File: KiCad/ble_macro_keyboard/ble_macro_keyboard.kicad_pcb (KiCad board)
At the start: 2 copper layers, 91 x 55 mm, 38 parts, among them IC1 ADP3338AKCZ-3.3-RL, J1 Conn_01x03_Male, Q1 IRLML6402, SW1 SW_SPDT, SW10 SW_Push, SW11 SW_Push, SW12 SW_Push, SW13 SW_Push, SW14 SW_Push, SW2 SW_Push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

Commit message: [fix] Vsysラベルを3.3vへ修正
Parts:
- moved C2 55.2 mm to (235.2, -128.5)
- moved C1 54.4 mm to (196.7, -114.3)
- moved R7 39.3 mm to (199.1, -111.8), turned to 0 degrees
- moved C4 33.8 mm to (197.6, -127.0), turned to 90 degrees
- moved C6 13.7 mm to (174.8, -113.8), turned to 0 degrees
- moved D2 10.2 mm to (208.8, -122.9)
- moved R3 10.2 mm to (201.8, -122.9)
- moved R4 10.2 mm to (198.0, -122.9)
- moved R1 10.2 mm to (201.8, -127.0)
- moved R2 10.2 mm to (201.7, -125.0)
- moved C5 9.71 mm to (186.5, -113.8), turned to 0 degrees
- moved D1 9.65 mm to (208.8, -115.8)
- moved R5 9.65 mm to (208.8, -113.3)
- moved IC1 6.68 mm to (191.0, -125.0)
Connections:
- C4 pad 1: Vsys -> +3.3V
- IC1 pad 2: Vsys -> +3.3V
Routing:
- net Net-(D2-Pad3): track 0.90 -> 0.00 mm

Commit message: [update] GND以外パターン接続
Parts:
- moved R5 39.5 mm to (171.3, -126.0)
- moved D1 39.2 mm to (172.2, -130.0), turned to 180 degrees
- moved R7 28.6 mm to (171.3, -118.4)
- moved C1 26.4 mm to (171.3, -121.4), turned to 0 degrees
- moved C6 23.7 mm to (192.1, -130.0)
- moved C5 17.6 mm to (179.8, -130.0), turned to 180 degrees
- moved IC1 16.2 mm to (204.7, -116.3)
- moved C2 14.7 mm to (243.3, -116.3), turned to 90 degrees
- moved R6 13.9 mm to (185.9, -131.1)
- moved U1 13.5 mm to (185.9, -127.5)
- moved C3 11.4 mm to (185.9, -118.4), turned to 0 degrees
- moved C4 9.04 mm to (204.7, -121.4), turned to 0 degrees
- moved Q1 8.64 mm to (185.9, -114.8)
- moved J1 6.62 mm to (238.8, -116.3), turned to 90 degrees
- moved R1 4.82 mm to (203.3, -131.6)
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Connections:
- U2 pad 10: LED_R -> KeySW_read_04
- U2 pad 11: KeySW_read_12 -> KeySW_read_08
- U2 pad 12: KeySW_read_08 -> KeySW_read_12
- U2 pad 15: KeySW_read_04 -> setSW_read
- U2 pad 7: setSW_read -> LED_G
- U2 pad 8: LED_G -> LED_B
- U2 pad 9: LED_B -> LED_R
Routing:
- net KeySW_read_12: track 0.00 -> 136.6 mm
- net KeySW_read_08: track 0.00 -> 113.3 mm
- net Net-(C2-Pad1): track 0.00 -> 97.2 mm
- net KeySW_read_04: track 0.00 -> 90.5 mm
- net Net-(C3-Pad1): track 0.00 -> 79.0 mm, vias 0 -> 1
- net +5V: track 0.00 -> 70.3 mm, vias 0 -> 2
- net setSW_read: track 0.00 -> 68.7 mm
- net KeySW_read_11: track 0.00 -> 65.8 mm
- net KeySW_read_10: track 0.00 -> 58.4 mm
- net Net-(IC1-Pad3): track 0.00 -> 57.5 mm, vias 0 -> 1
- net KeySW_read_09: track 0.00 -> 53.1 mm
- net Battery_thermistor: track 0.00 -> 53.1 mm
- net KeySW_read_07: track 0.00 -> 40.3 mm
- net KeySW_read_06: track 0.00 -> 36.2 mm
- net +3.3V: track 0.00 -> 35.3 mm
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
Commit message: [add] ライブラリ及び回路図にNPTH_8mmを追加
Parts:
- added REF**: NPTH_8mm, Ble_keyboard:NPTH_8mm, F.Cu at (19.0, -32.0)
- moved REF** 233.1 mm to (40.0, 46.0)
- moved REF** 232.9 mm to (-40.0, 46.0)
- moved REF** 231.5 mm to (40.0, -41.0)
- moved REF** 231.3 mm to (-40.0, -41.0)
- moved C1 231.1 mm to (-37.4, -22.4)
- moved C2 231.1 mm to (34.5, -17.3)
- moved C3 231.1 mm to (-22.9, -19.3)
- moved C5 231.1 mm to (-29.0, -31.0)
- moved C6 231.1 mm to (-16.7, -31.0)
- moved D2 231.1 mm to (0.00, -28.4)
- moved Q1 231.1 mm to (-22.9, -15.7)
- moved R1 231.1 mm to (-5.45, -32.5)
- moved R3 231.1 mm to (-5.45, -28.4)
- moved R4 231.1 mm to (-9.26, -28.4)
- moved R6 231.1 mm to (-22.9, -32.0)
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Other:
- board size 91 x 55 mm -> 88 x 95 mm

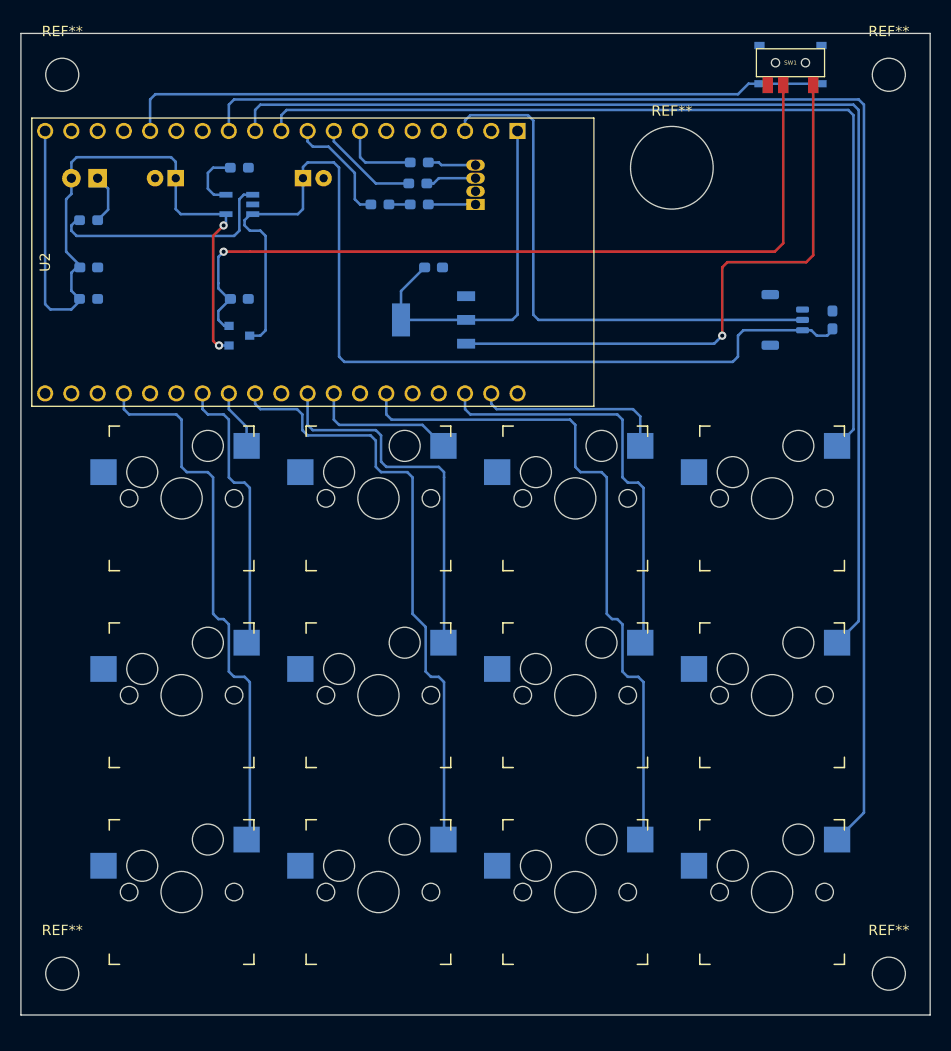
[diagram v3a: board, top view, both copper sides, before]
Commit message: [fix] Ble_keyboardフットプリントライブラリのSWがGNDに接続するように解決
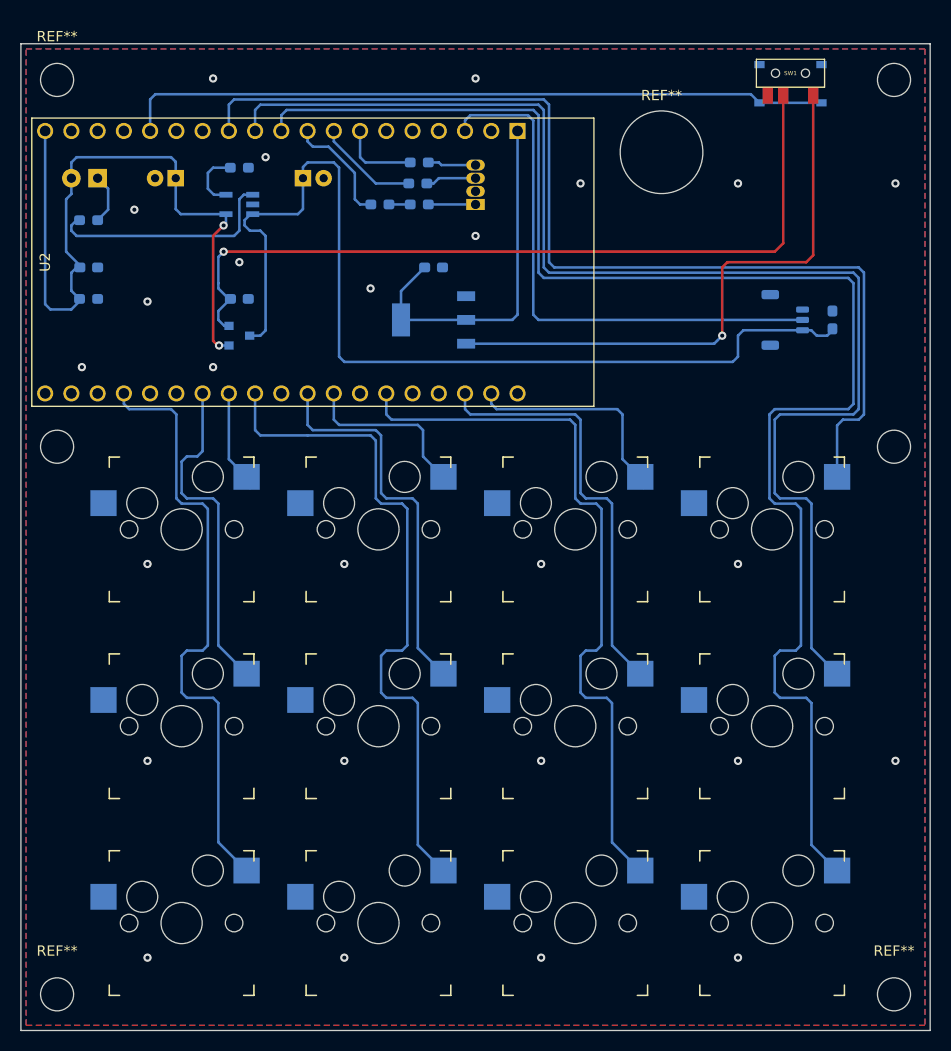
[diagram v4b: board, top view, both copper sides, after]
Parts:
- added REF**: MountingHole_3.2mm_M3, MountingHole:MountingHole_3.2mm_M3, F.Cu at (40.5, -5.00)
- added REF**: MountingHole_3.2mm_M3, MountingHole:MountingHole_3.2mm_M3, F.Cu at (-40.5, -5.00)
- moved SW10 3.00 mm to (28.7, 22.1)
- moved SW11 3.00 mm to (-28.4, 41.1)
- moved SW12 3.00 mm to (-9.40, 41.1)
- moved SW13 3.00 mm to (9.65, 41.1)
- moved SW14 3.00 mm to (28.7, 41.1)
- moved SW3 3.00 mm to (-28.4, 3.00)
- moved SW4 3.00 mm to (-9.40, 3.00)
- moved SW5 3.00 mm to (9.65, 3.00)
- moved SW6 3.00 mm to (28.7, 3.00)
- moved SW7 3.00 mm to (-28.4, 22.1)
- moved SW8 3.00 mm to (-9.40, 22.1)
- moved SW9 3.00 mm to (9.65, 22.1)
- moved REF** 2.06 mm to (-40.5, 48.0)
- moved REF** 2.06 mm to (40.5, 48.0)
- moved SW2 1.85 mm to (30.5, -40.1)
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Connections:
- U2 pad 10: KeySW_read_04 -> KeySW_read_12
- U2 pad 12: KeySW_read_12 -> KeySW_read_04
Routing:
- net KeySW_read_08: track 113.3 -> 126.4 mm
- net KeySW_read_04: track 90.5 -> 101.8 mm
- net KeySW_read_12: track 136.6 -> 146.3 mm
- net KeySW_read_10: track 58.4 -> 65.7 mm
- net KeySW_read_09: track 53.1 -> 59.2 mm
- net KeySW_read_05: track 27.6 -> 32.7 mm
- net KeySW_read_11: track 65.8 -> 70.8 mm
- net KeySW_read_01: track 5.79 -> 9.51 mm
- net KeySW_read_02: track 14.2 -> 17.4 mm
- net KeySW_read_03: track 18.8 -> 21.6 mm
- net KeySW_read_06: track 36.2 -> 38.4 mm
- net KeySW_read_07: track 40.3 -> 42.0 mm
- net Net-(IC1-Pad3): track 57.5 -> 56.5 mm
- net Net-(C3-Pad1): track 79.0 -> 77.9 mm
- net GND: vias 0 -> 26
- added copper zone on B.Cu, net GND
- added copper zone on F.Cu, net GND
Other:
- board size 88 x 95 mm -> 88 x 95.5 mm

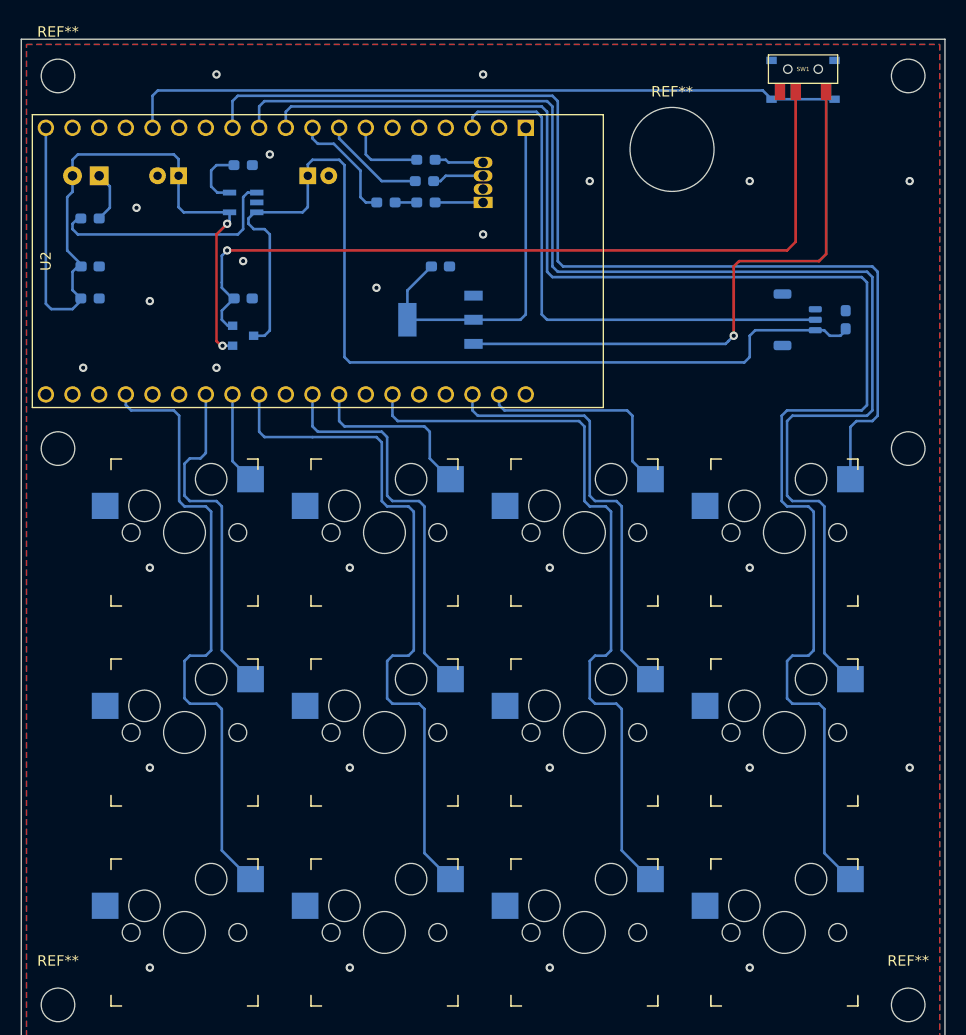
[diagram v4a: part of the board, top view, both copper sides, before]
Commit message: [fix] Ble_keyboardライブラリのシルクスクリーンとパッドが干渉するライブラリを修正
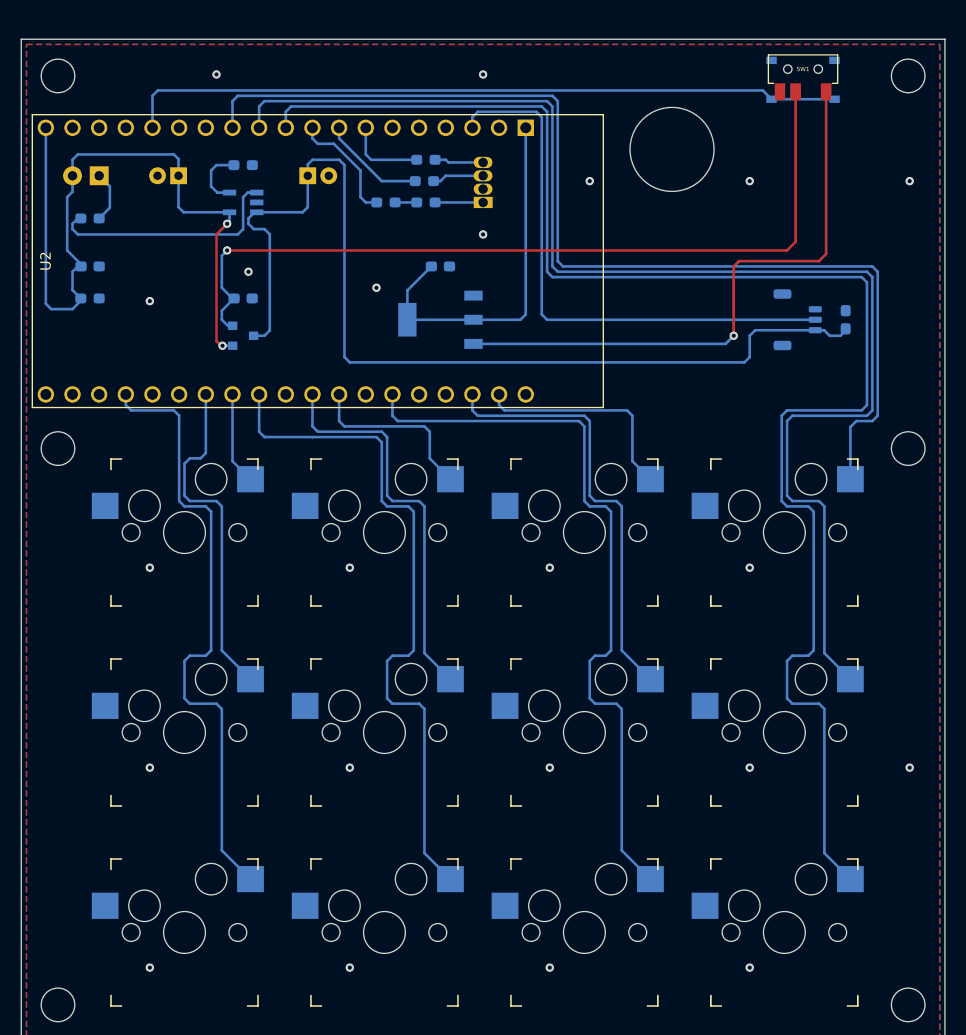
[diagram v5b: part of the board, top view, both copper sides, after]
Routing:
- net KeySW_read_06: track 38.4 -> 37.6 mm
- net KeySW_read_03: track 21.6 -> 20.9 mm
- net KeySW_read_01: track 9.51 -> 8.79 mm
- net KeySW_read_07: track 42.0 -> 41.3 mm
- net KeySW_read_12: track 146.3 -> 145.7 mm
- net LED_R: track 11.7 -> 11.2 mm
- net LED_B: track 10.5 -> 9.95 mm
- net KeySW_read_02: track 17.4 -> 16.9 mm
- net GND: vias 26 -> 22

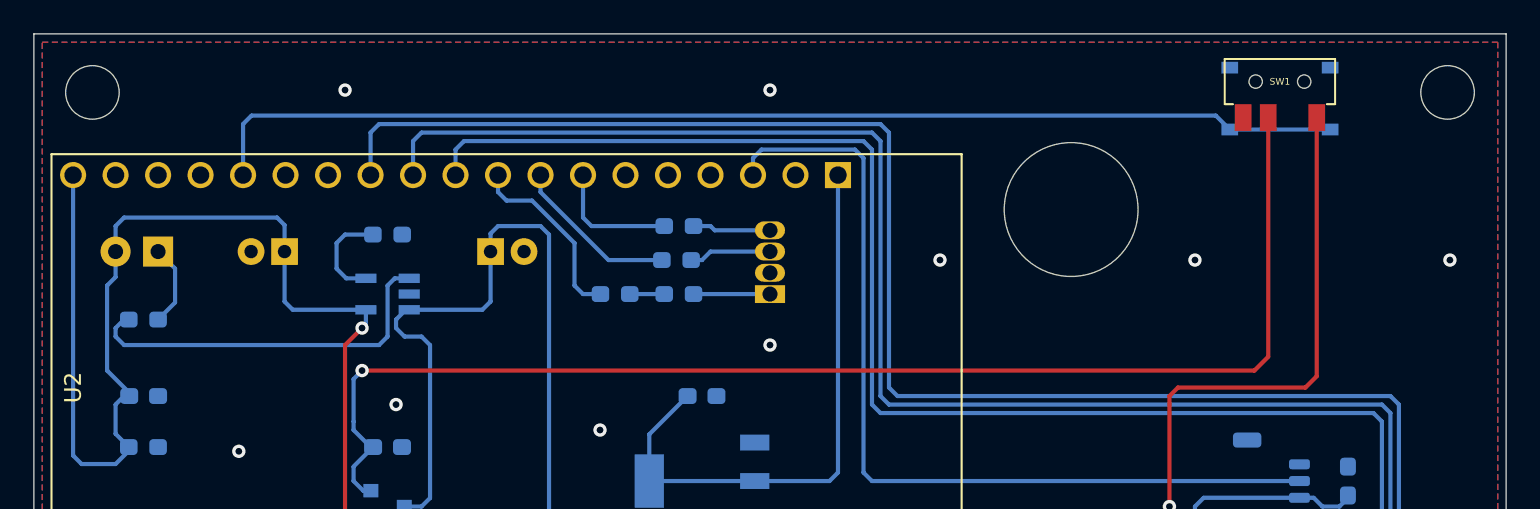
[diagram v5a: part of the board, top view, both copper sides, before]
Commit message: [add] 底板の図面出力
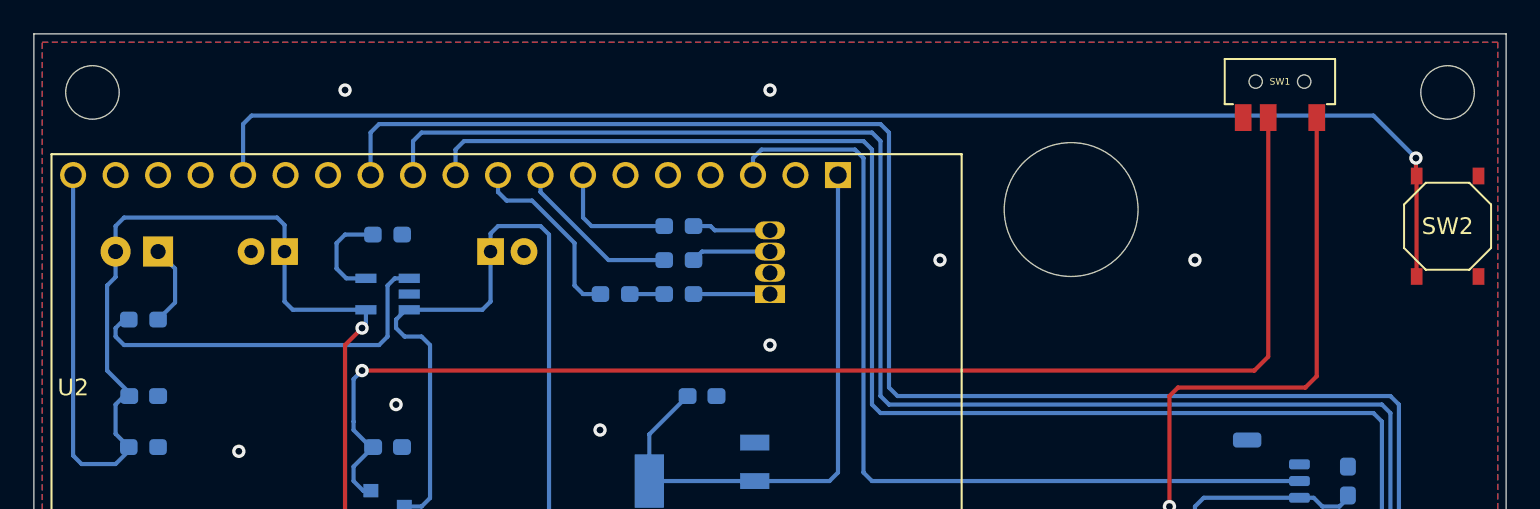
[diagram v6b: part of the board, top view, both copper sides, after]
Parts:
- SW2: moved to F.Cu
- moved SW2 12.6 mm to (40.5, -32.5), turned to 90 degrees
- moved R2 0.14 mm to (-5.45, -30.5)
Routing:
- net setSW_read: track 68.6 -> 81.5 mm, vias 0 -> 1
- net GND: vias 22 -> 21
